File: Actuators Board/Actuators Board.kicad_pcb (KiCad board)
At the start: 4 copper layers, 50 x 50 mm, 132 parts, among them IC1 BD62120AEFJ-E2, J1 Conn_01x05_Male, J10 Conn_01x02_Male, J2 Solenoid(Sol), J3 USB_C_Receptacle_USB2.0, J4 Conn_01x03_Male, J5 Conn_01x06_Male, J6 Conn_01x02_Female, J9 Conn_01x02_Male, Q1 MMDT2222A, Q2 SI2366DS, U1 ESP32-PICO-D4, U2 TPS54233D, U3 CP2102-GMR-QFN28, U4 SN65HVD230, U5 LTC4411, U6 RT9025-25GSP, U7 LTC4411

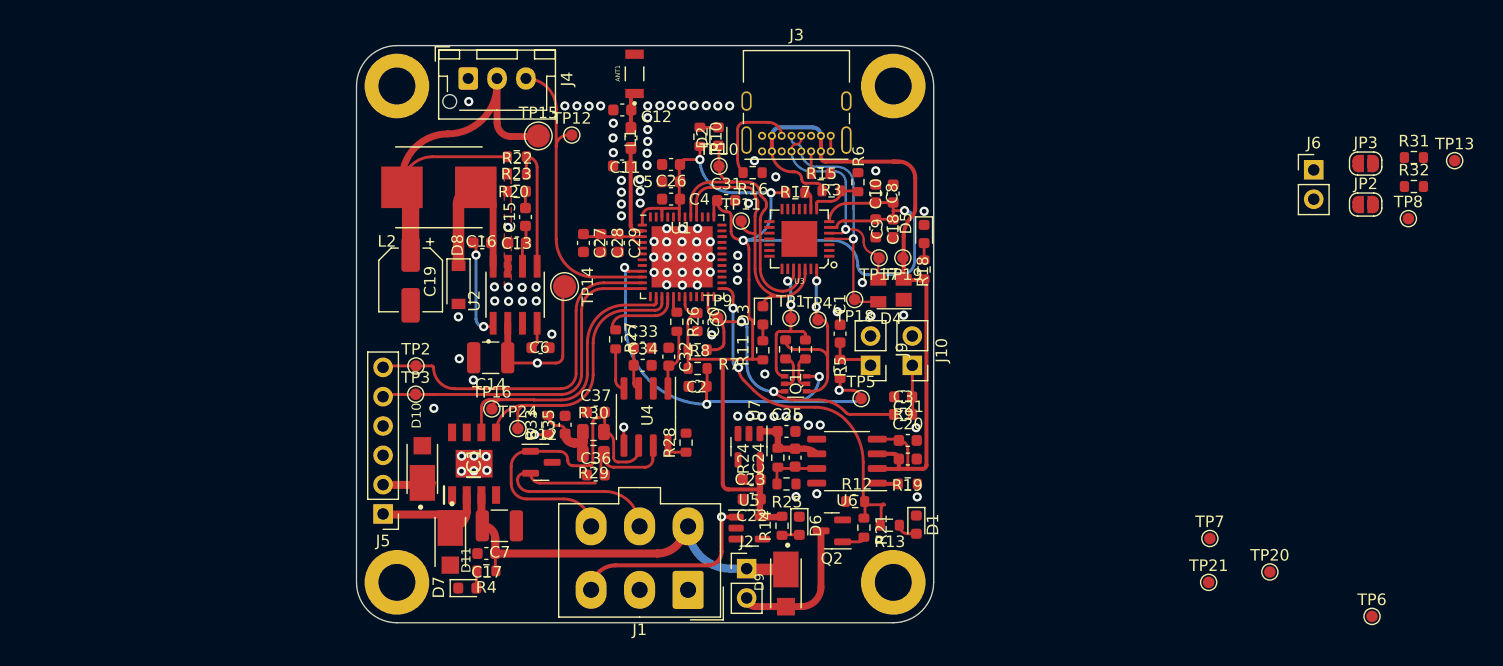
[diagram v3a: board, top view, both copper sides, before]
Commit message: Changed connectors
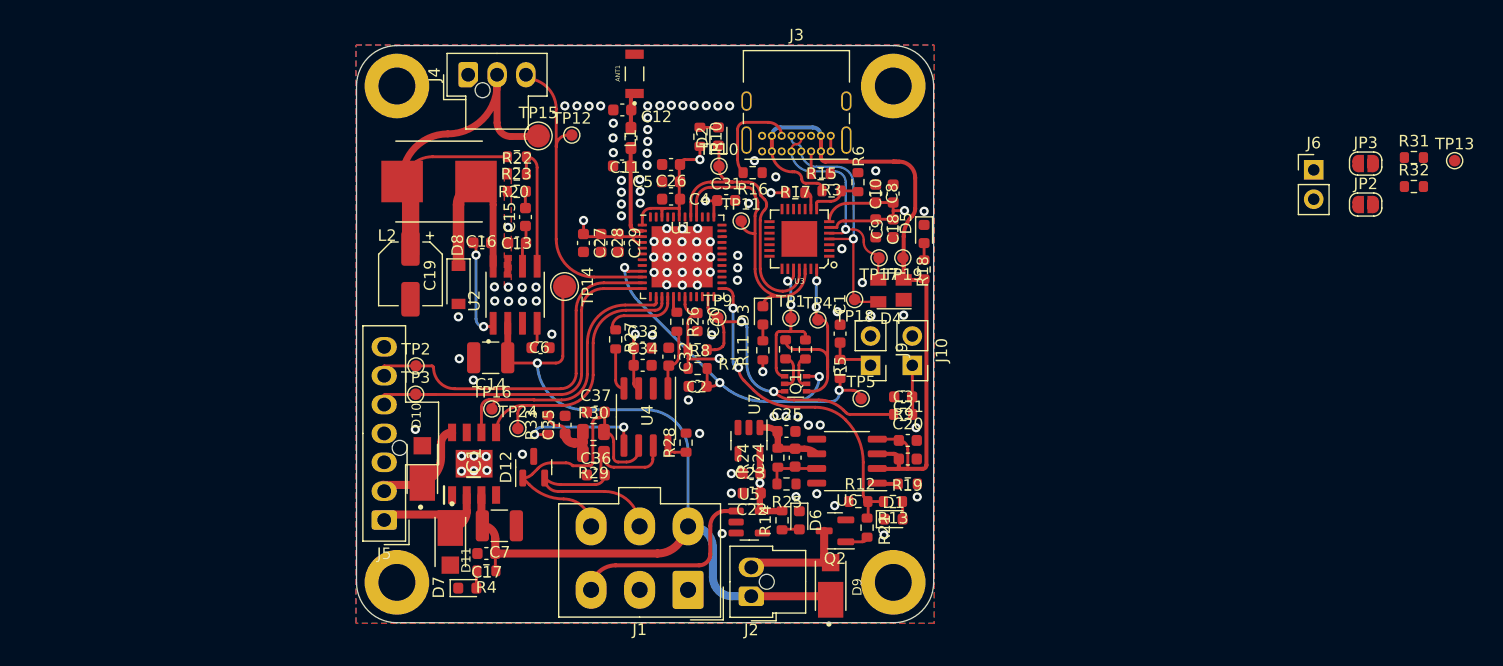
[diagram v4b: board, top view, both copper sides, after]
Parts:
- removed ?: , 
- removed TP20, TP21, TP6, TP7, TP8: TestPoint, TestPoint:TestPoint_Pad_D1.0mm
- J2: footprint Connector_PinHeader_2.54mm:PinHeader_1x02_P2.54mm_Vertical -> Connector_Molex:Molex_Nano-Fit_105309-xx02_1x02_P2.50mm_Vertical
- J4: footprint Connector_JST:JST_XH_B3B-XH-AM_1x03_P2.50mm_Vertical -> Connector_Molex:Molex_Nano-Fit_105309-xx03_1x03_P2.50mm_Vertical
- J5: footprint Connector_PinHeader_2.54mm:PinHeader_1x06_P2.54mm_Vertical -> Connector_Molex:Molex_Nano-Fit_105309-xx07_1x07_P2.50mm_Vertical
- moved D9 3.88 mm to (96.1, 76.8), turned to 90 degrees
- moved J2 2.42 mm to (89.2, 77.7), turned to 180 degrees
- moved R13 2.07 mm to (101.5, 69.5)
- moved D1 2.03 mm to (101.5, 71.0), turned to 0 degrees
- moved D12 0.79 mm to (70.3, 66.5), turned to 90 degrees
- moved J5 0.53 mm to (57.4, 71.1)
- moved C19 0.53 mm to (59.7, 49.8)
- moved U7 0.53 mm to (89.0, 64.2)
- moved C22 0.52 mm to (89.2, 68.8)
- moved C23 0.52 mm to (89.2, 67.1)
- moved U5 0.52 mm to (89.0, 71.3)
- moved L2 0.50 mm to (62.1, 41.8)
- moved D6 0.47 mm to (93.4, 71.1)
- moved R14 0.47 mm to (91.9, 71.1)
- moved J4 0.33 mm to (64.7, 32.5), turned to 90 degrees
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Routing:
- net +3V3: track 124.1 -> 60.9 mm, vias 4 -> 9
- net +24V: track 50.8 -> 80.1 mm
- net /CAN-BUS/Vref: track 2.77 -> 10.8 mm
- net /EN: track 42.2 -> 37.3 mm
- net /CAN_LOW: track 32.5 -> 27.7 mm
- net /Motor-: track 4.43 -> 8.96 mm
- net /CAN_HIGH: track 29.1 -> 25.1 mm
- net /SolGND: track 12.6 -> 10.1 mm
- net /SolEN: track 31.5 -> 29.4 mm
- net Net-(J1-Pad3): vias 1 -> 0
- net GND: vias 95 -> 100
- added copper zone on B.Cu, net GND

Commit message: Finished Board Layout
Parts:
- removed J6: Conn_01x02_Female, Connector_PinHeader_2.54mm:PinHeader_1x02_P2.54mm_Vertical
- removed JP2: Pull-Down, Jumper:SolderJumper-2_P1.3mm_Open_RoundedPad1.0x1.5mm
- removed JP3: Pull-Up, Jumper:SolderJumper-2_P1.3mm_Open_RoundedPad1.0x1.5mm
- added R34: 10k, Resistor_SMD:R_0603_1608Metric, F.Cu at (85.0, 61.9)
- added R35: 10k, Resistor_SMD:R_0603_1608Metric, F.Cu at (85.0, 65.0)
- added TP22: TestPoint, TestPoint:TestPoint_Pad_D1.5mm, F.Cu at (87.4, 60.6)
- added TP25: TestPoint, TestPoint:TestPoint_Pad_D1.5mm, F.Cu at (82.7, 66.9)
- added TP8: TestPoint, TestPoint:TestPoint_Pad_D1.5mm, F.Cu at (74.8, 39.8)
- J5: footprint Connector_Molex:Molex_Nano-Fit_105309-xx07_1x07_P2.50mm_Vertical -> Connector_Molex:Molex_Nano-Fit_105309-xx06_1x06_P2.50mm_Vertical
- moved R31 71.9 mm to (74.8, 42.7), turned to -90 degrees
- moved R32 69.9 mm to (77.0, 47.9)
- moved TP13 62.3 mm to (88.4, 48.2)
- moved D7 4.19 mm to (68.5, 78.7)
- moved TP3 3.68 mm to (63.6, 61.3)
- moved R4 2.75 mm to (68.5, 77.2), turned to 0 degrees
- moved D10 2.35 mm to (61.3, 69.0), turned to -90 degrees
- moved J5 2.10 mm to (57.4, 69.0)
- moved D11 2.07 mm to (63.4, 75.1)
- moved C17 1.74 mm to (66.8, 75.6)
- moved C7 1.74 mm to (68.0, 73.2)
- moved IC1 1.47 mm to (65.8, 67.5)
- moved C27 1.42 mm to (74.8, 45.7), turned to 90 degrees
- moved C28 1.42 mm to (76.2, 45.7), turned to 90 degrees
- moved C29 1.42 mm to (77.7, 45.7), turned to 90 degrees
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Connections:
- IC1 pad 9: GND -> (no net)
- R31 pad 1: Net-(JP2-Pad2) -> /SSRGPIO
- R32 pad 2: Net-(JP3-Pad2) -> /SSRGPIO
- TP13 pad 1: /SSRGPIO -> /SolEN
- U1 pad 25: /SolEN -> /ES1GPIO
- U1 pad 27: /SSRGPIO -> /ES2GPIO
- U1 pad 28: unconnected-(U1-Pad28) -> /SolEN
- U1 pad 6: unconnected-(U1-Pad6) -> /SSRGPIO
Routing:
- net /ES2GPIO: track 0.00 -> 21.7 mm
- net /SSRGPIO: track 0.00 -> 16.2 mm
- net /ES1GPIO: track 0.00 -> 14.3 mm
- net GND: track 1.72 -> 6.47 mm, vias 100 -> 112
- net /Motor+: track 10.2 -> 14.7 mm
- net /SolEN: track 29.4 -> 33.6 mm, vias 2 -> 0
- net +3V3: track 60.9 -> 64.7 mm, vias 9 -> 10
- net /BOOT: track 28.4 -> 25.4 mm
- net /Hall2: track 31.0 -> 32.3 mm
- net /Motor-: track 8.96 -> 10.1 mm
- net /Hall1: track 30.6 -> 31.6 mm
- net /ServoPWM: track 26.4 -> 27.2 mm
- net /HBridgeDIR1: track 24.6 -> 25.2 mm

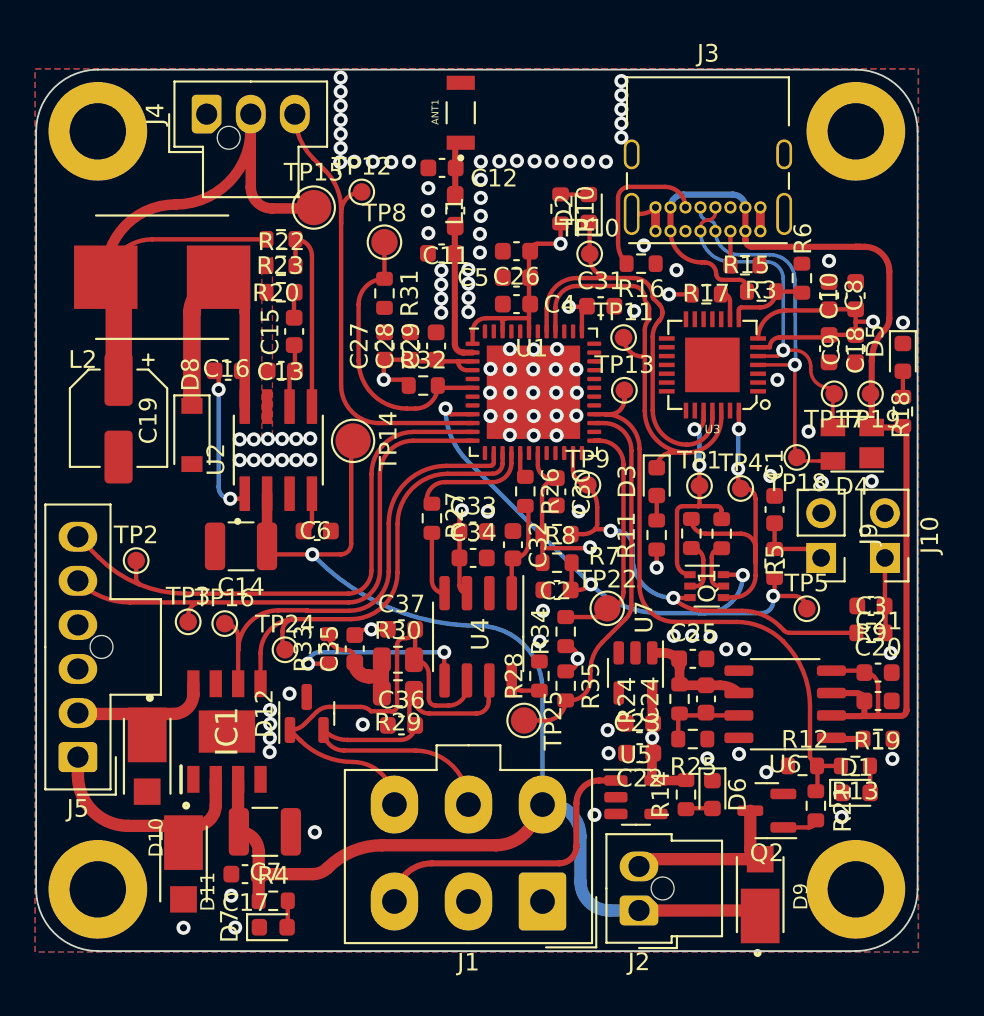
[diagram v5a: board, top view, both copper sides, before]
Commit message: Swapped SSR pad for connector
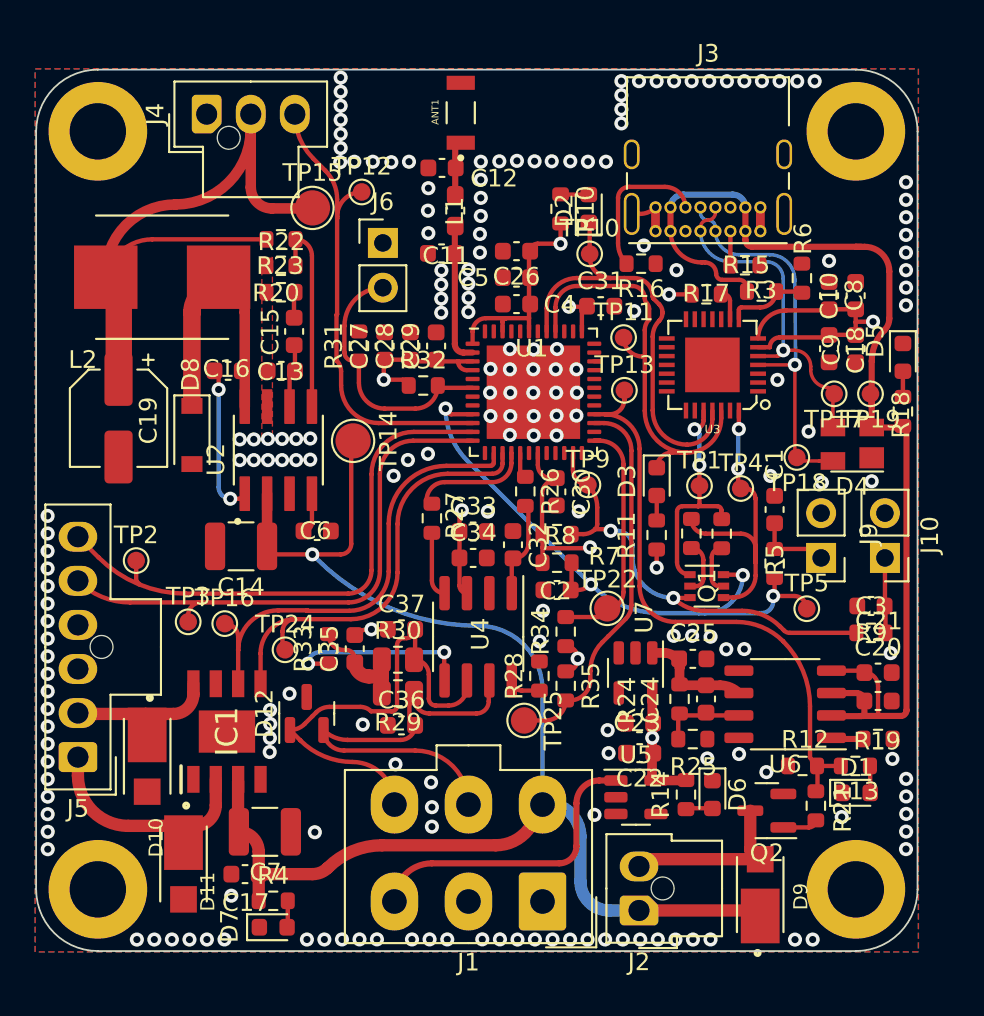
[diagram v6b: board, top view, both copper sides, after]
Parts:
- removed TP8: TestPoint, TestPoint:TestPoint_Pad_D1.5mm
- added J6: Conn_01x02_Male, Connector_PinHeader_2.54mm:PinHeader_1x02_P2.54mm_Vertical, F.Cu at (74.7, 39.8)
- moved R31 3.32 mm to (73.3, 45.7), turned to 90 degrees
- moved TP15 0.08 mm to (70.7, 37.8)
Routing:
- net /SSRGPIO: track 16.2 -> 15.2 mm
- net GND: vias 112 -> 189

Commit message: Fixed front silkscreen (references) and added ICLR logo + designer names
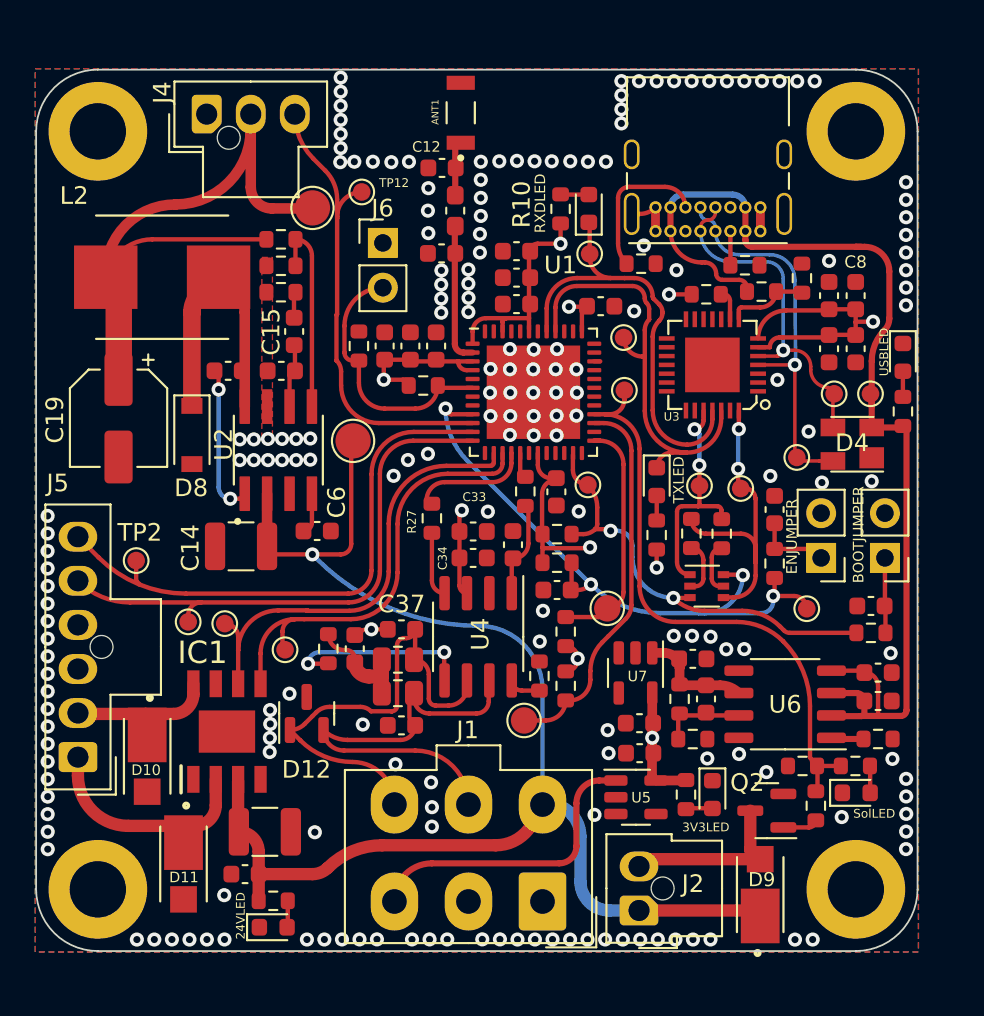
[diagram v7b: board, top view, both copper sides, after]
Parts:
- added G***: LOGO, iclr:iclr_logo, B.Cu at (62.0, 41.3)
- renumbered D7 to 24VLED, D6 to 3V3LED, J10 to BOOTJUMPER, J9 to ENJUMPER, D2 to RXDLED, D1 to SolLED, D3 to TXLED, D5 to USBLED
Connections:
- IC1 pad 9: (no net) -> GND
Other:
- board text added: "Designed By Andrei Paduraru Aleks Kent"
- board text added: "Electronics and Paylod ICLR"

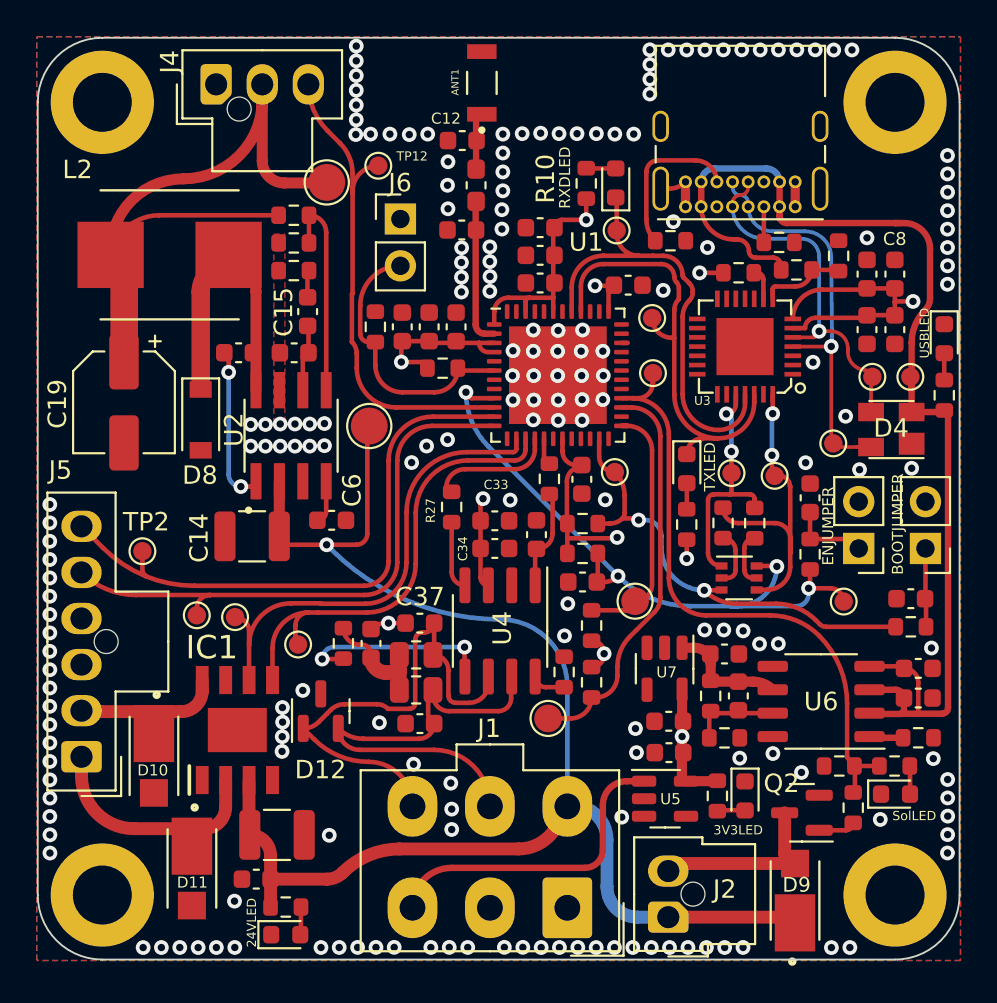
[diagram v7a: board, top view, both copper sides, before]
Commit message: Added board name and picture, rerouted USB traces
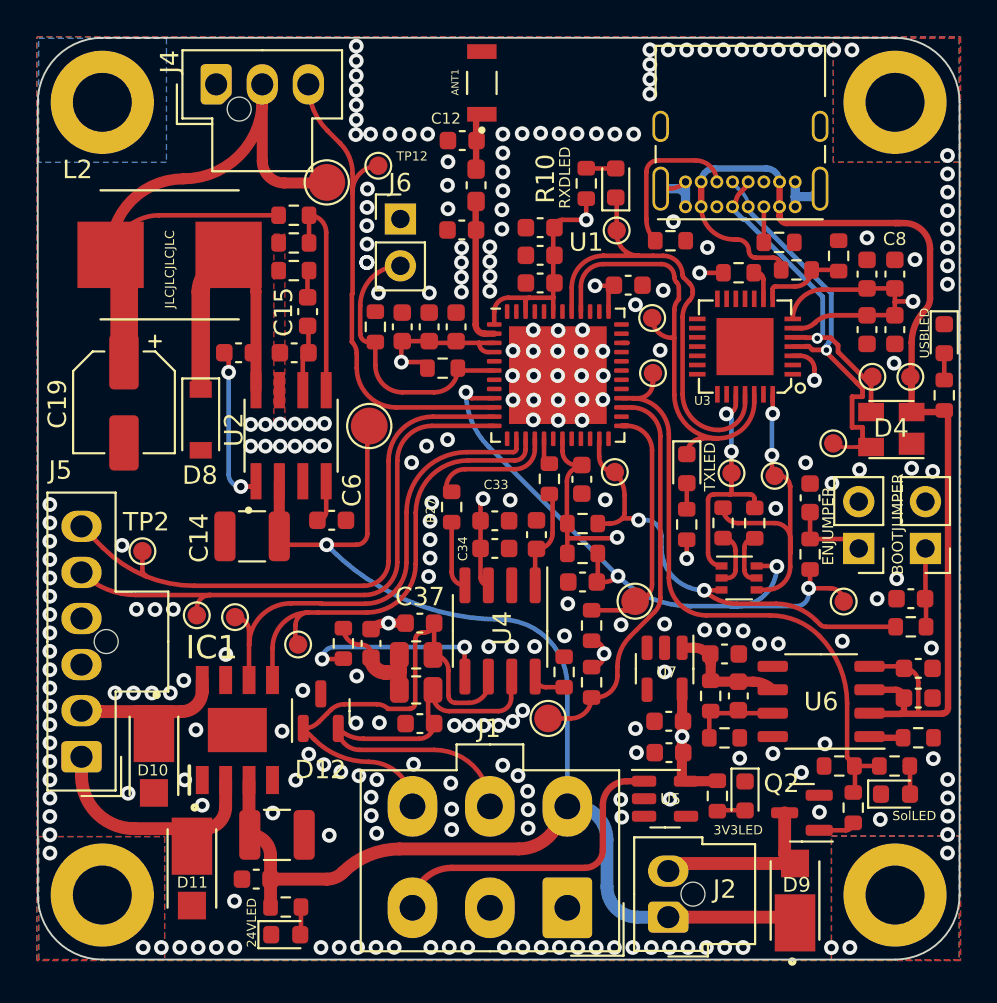
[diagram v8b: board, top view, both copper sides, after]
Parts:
- added G***: LOGO, LOGO, B.Cu at (80.4, 49.0)
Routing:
- net GND: track 6.47 -> 11.6 mm, vias 189 -> 256
- net /USB -> UART/Data+: track 21.9 -> 22.9 mm
- net /USB -> UART/Data-: track 19.5 -> 20.3 mm
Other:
- board text added: "C - CAN H - H-Bridge A - Actuator D - DC"
- board text added: "C.H.A.D - v1"
- board text added: "Designed By Andrei Paduraru Aleks Kent Electronics And Payload 2022"
- board text added: "JLCJLCJLCJLC"
- board text removed: "Designed By Andrei Paduraru Aleks Kent"
- board text removed: "Electronics and Paylod ICLR"
